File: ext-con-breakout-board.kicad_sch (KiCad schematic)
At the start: 6 parts, among them J1 Conn_02x12_Odd_Even, J2 Conn_01x03, J3 Conn_01x03, J4 Conn_01x03, J5 Conn_01x05, J6 Conn_01x03

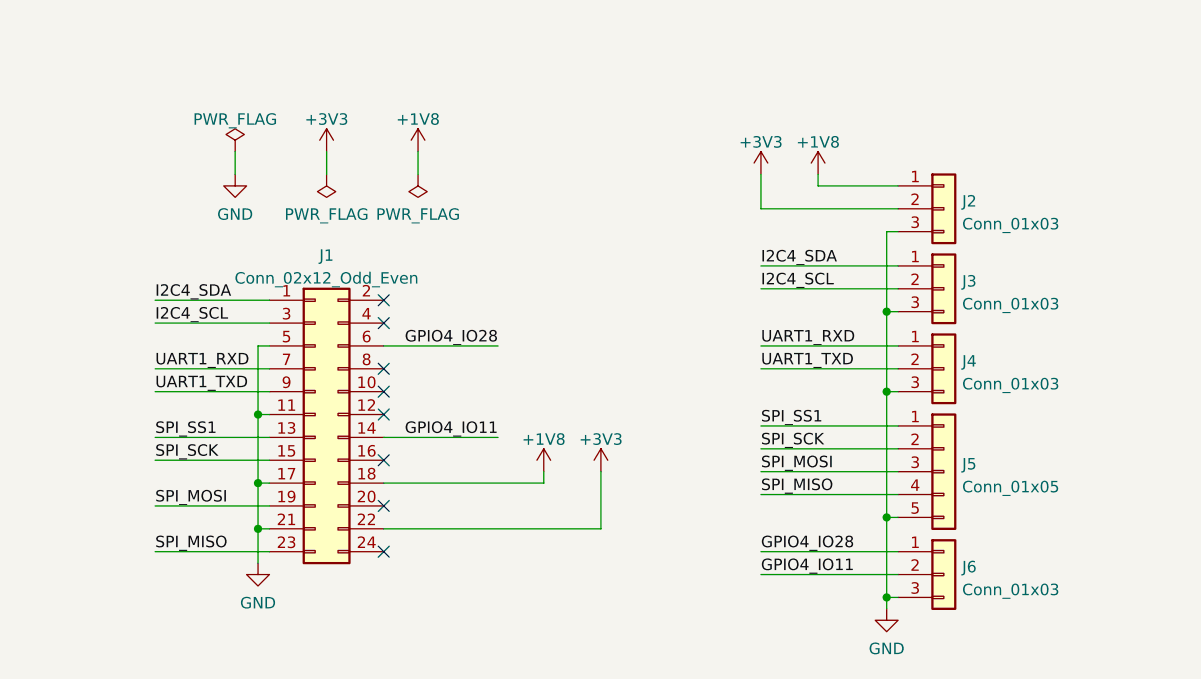
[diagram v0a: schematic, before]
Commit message: Begin fanning out the nets near the FPC connector
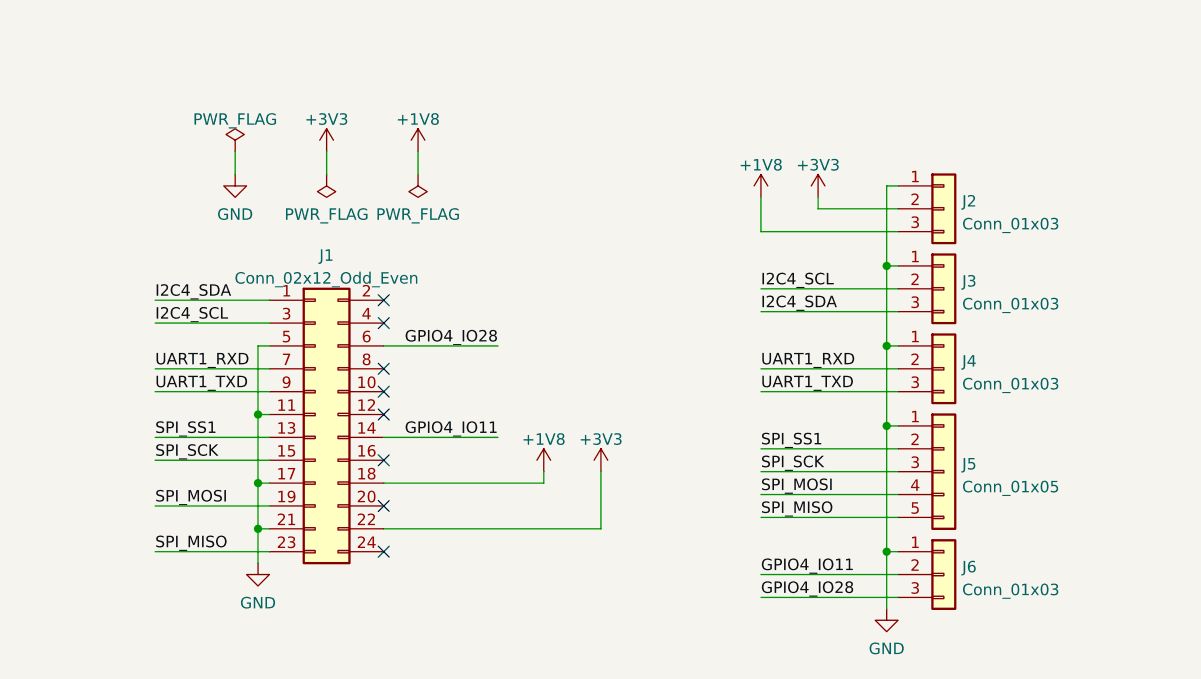
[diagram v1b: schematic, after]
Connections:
- net +1V8: now also J2.3 (Pin_3); no longer J2.1 (Pin_1)
- net GND: now also J2.1 (Pin_1), J3.1 (Pin_1), J4.1 (Pin_1), J5.1 (Pin_1), J6.1 (Pin_1); no longer J2.3 (Pin_3), J3.3 (Pin_3), J4.3 (Pin_3), J5.5 (Pin_5), J6.3 (Pin_3)
- net GPIO4_IO28: now also J6.3 (Pin_3); no longer J6.1 (Pin_1)
- net I2C4_SDA: now also J3.3 (Pin_3); no longer J3.1 (Pin_1)
- net SPI_MISO: now also J5.5 (Pin_5); no longer J5.4 (Pin_4)
- net SPI_MOSI: now also J5.4 (Pin_4); no longer J5.3 (Pin_3)
- net SPI_SCK: now also J5.3 (Pin_3); no longer J5.2 (Pin_2)
- net SPI_SS1: now also J5.2 (Pin_2); no longer J5.1 (Pin_1)
- net UART1_RXD: now also J4.2 (Pin_2); no longer J4.1 (Pin_1)
- net UART1_TXD: now also J4.3 (Pin_3); no longer J4.2 (Pin_2)

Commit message: Route the remaining portion of the FPC section and add the rigid section
The rigid section has a mounting hole which lines up with the center
screw that holds the M.2 cover in place. This will allow the board to be
mounted to the back of the phone.

Extra flex length was given to ensure enough distance to reach the
position where the rigid section will be mounted. The drawings on the
User.1 layer shows where the plastic obstacles are as well as the
location of the M1.4 threaded hole. There is approximately 5.4mm of
additional slack in the length of the flex section so that it can be
tucked inside the volume it runs along.

The rigid section of the board will sit between the M.2 modules, on top
of the ~10.5mm plastic section that separates the two. The rigid section
has a 7mm and should close to the center of the plastic divider.
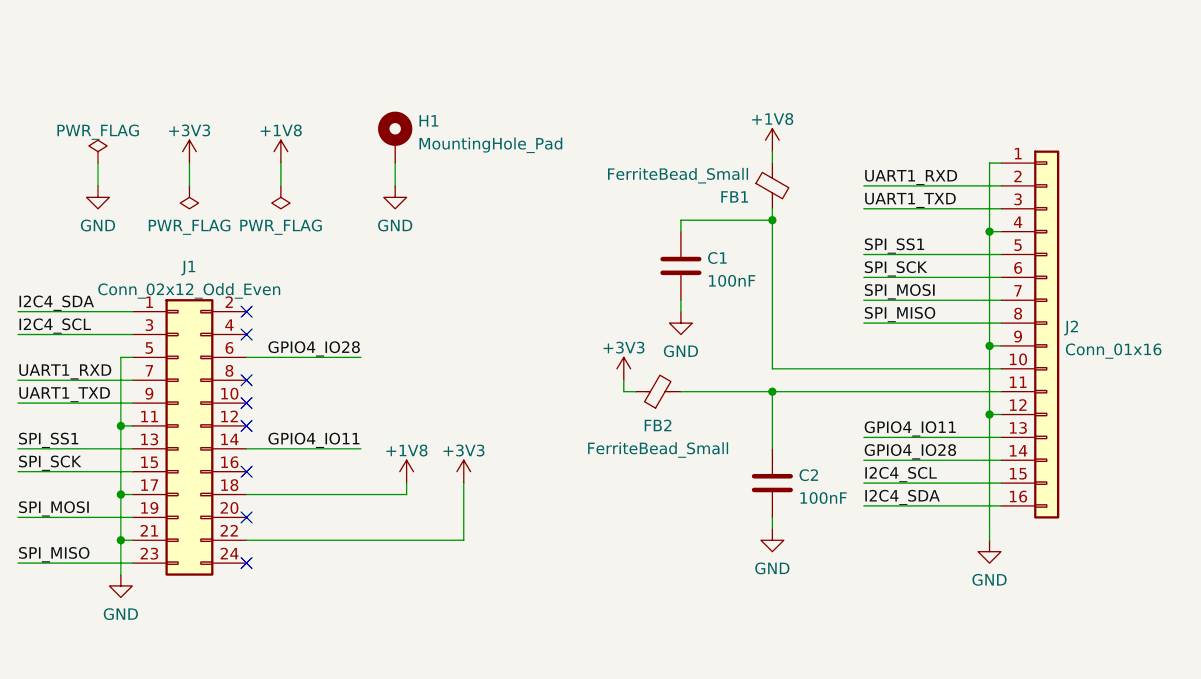
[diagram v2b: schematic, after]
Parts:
- removed J2, J3, J4, J6: Conn_01x03, Connector_PinHeader_2.54mm:PinHeader_1x03_P2.54mm_Vertical, symbol Connector_Generic:Conn_01x03
- removed J5: Conn_01x05, Connector_PinHeader_2.54mm:PinHeader_1x05_P2.54mm_Vertical, symbol Connector_Generic:Conn_01x05
- added C1, C2: 100nF, Capacitor_SMD:C_0402_1005Metric, symbol Device:C
- added FB1, FB2: FerriteBead_Small, Inductor_SMD:L_0402_1005Metric, symbol Device:FerriteBead_Small
- added H1: MountingHole_Pad, ext-con-breakout-board:MountingHole_1.7mm_M1.4_Pad, symbol Mechanical:MountingHole_Pad
- added J2: Conn_01x16, Connector_PinHeader_2.54mm:PinHeader_1x16_P2.54mm_Vertical, symbol Connector_Generic:Conn_01x16
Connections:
- net +1V8: now also FB1.1
- net +3V3: now also FB2.1
- net GND: now also C1.2, C2.2, H1.1, J2.1 (Pin_1), J2.12 (Pin_12), J2.4 (Pin_4), J2.9 (Pin_9)
- net GPIO4_IO11: now also J2.13 (Pin_13)
- net GPIO4_IO28: now also J2.14 (Pin_14)
- net I2C4_SCL: now also J2.15 (Pin_15)
- net I2C4_SDA: now also J2.16 (Pin_16)
- net SPI_MISO: now also J2.8 (Pin_8)
- net SPI_MOSI: now also J2.7 (Pin_7)
- net SPI_SCK: now also J2.6 (Pin_6)
- net SPI_SS1: now also J2.5 (Pin_5)
- net UART1_RXD: now also J2.2 (Pin_2)
- net UART1_TXD: now also J2.3 (Pin_3)
- new net: C2.1, FB2.2, J2.11 (Pin_11)
- new net: C1.1, FB1.2, J2.10 (Pin_10)
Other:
- moved on the sheet: J1

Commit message: Export the manufacturing files (gerbers and PDF)
Add fab notes on the User.Comments layer. Include a general stackup
guide image in the PDF fabrication drawing.

Re-centered the whole board on the canvas. The vias on the flex section
have to be set as "buried" vias going from In1.Cu to In2.Cu in order to
get the correct gerber export.
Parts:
- added FID1, FID2: Fiducial, ext-con-breakout-board:Fiducial_0.5mm_Mask1mm, symbol Mechanical:Fiducial
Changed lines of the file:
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@@
     (pin "1")
+  )
+  (symbol (lib_id "Mechanical:Fiducial") (at 134.62 53.34 0) (unit 1)
+    (in_bom yes) (on_board yes) (fields_autoplaced)
+    (property "Reference" "FID1" (id 0) (at 136.779 52.5053 0)
+      (effects (font (size 1.27 1.27)) (justify left))
+    )
+    (property "Value" "Fiducial" (id 1) (at 136.779 55.0422 0)
+      (effects (font (size 1.27 1.27)) (justify left))
+    )
+    (property "Footprint" "ext-con-breakout-board:Fiducial_0.5mm_Mask1mm" (id 2) (at 134.62 53.34 0)
+      (effects (font (size 1.27 1.27)) hide)
+    )
+    (property "Datasheet" "~" (id 3) (at 134.62 53.34 0)
+      (effects (font (size 1.27 1.27)) hide)
+    )
   )
   (symbol (lib_id "power:+1V8") (at 135.89 102.87 0) (unit 1)
@@
     )
     (pin "1")
+  )
+  (symbol (lib_id "Mechanical:Fiducial") (at 134.62 58.42 0) (unit 1)
+    (in_bom yes) (on_board yes) (fields_autoplaced)
+    (property "Reference" "FID2" (id 0) (at 136.779 57.5853 0)
+      (effects (font (size 1.27 1.27)) (justify left))
+    )
+    (property "Value" "Fiducial" (id 1) (at 136.779 60.1222 0)
+      (effects (font (size 1.27 1.27)) (justify left))
+    )
+    (property "Footprint" "ext-con-breakout-board:Fiducial_0.5mm_Mask1mm" (id 2) (at 134.62 58.42 0)
+      (effects (font (size 1.27 1.27)) hide)
+    )
+    (property "Datasheet" "~" (id 3) (at 134.62 58.42 0)
+      (effects (font (size 1.27 1.27)) hide)
+    )
   )
   (symbol (lib_id "power:GND") (at 176.53 107.95 0) (unit 1)
@@
       (reference "FB2") (unit 1) (value "FerriteBead_Small") (footprint "Inductor_SMD:L_0402_1005Metric")
     )
+    (path "/348e1a08-d960-49f7-a4c2-2406ebb9e7f7"
+      (reference "FID1") (unit 1) (value "Fiducial") (footprint "ext-con-breakout-board:Fiducial_0.5mm_Mask1mm")
+    )
+    (path "/8b0f9d29-928e-4593-b915-7eced46b9aef"
+      (reference "FID2") (unit 1) (value "Fiducial") (footprint "ext-con-breakout-board:Fiducial_0.5mm_Mask1mm")
+    )
     (path "/de90e809-d499-46e7-94be-b9a4383c59c0"
